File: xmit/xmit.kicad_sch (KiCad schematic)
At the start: 38 parts

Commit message: First round WIP on the filters and amplifier
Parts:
- removed C1, C13, C2: 1n, symbol Device:C
- removed C10: 9p, symbol Device:C
- removed C11, C3: 120p, symbol Device:C
- removed C12, C4: 50p, symbol Device:C
- removed C14, C18: 220p, symbol Device:C
- removed C15: 12p, symbol Device:C
- removed C16: 330p, symbol Device:C
- removed C17: 31p, symbol Device:C
- removed C5: 8.1p, symbol Device:C
- removed C6: 3.9p, symbol Device:C
- removed C7: 200p, symbol Device:C
- removed C8: 81p, symbol Device:C
- removed C9: 18p, symbol Device:C
- removed L1, L3: 1600n, symbol Device:L
- removed L2, L4: 800n, symbol Device:L
- removed L5: 2200n, symbol Device:L
- removed L6: 2000n, symbol Device:L
- removed R10, R11, R14, R15, R4, R5: 1e9, symbol Device:R
- removed R12, R6: 10, symbol Device:R
- removed R13, R3, R9: 10k, symbol Device:R
- removed R7: 150, symbol Device:R
- removed R8: 200, symbol Device:R
- removed V2: VPULSE, symbol Simulation_SPICE:VPULSE
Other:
- added sheet power (power.kicad_sch)
- added sheet transmit filters (filter.kicad_sch)

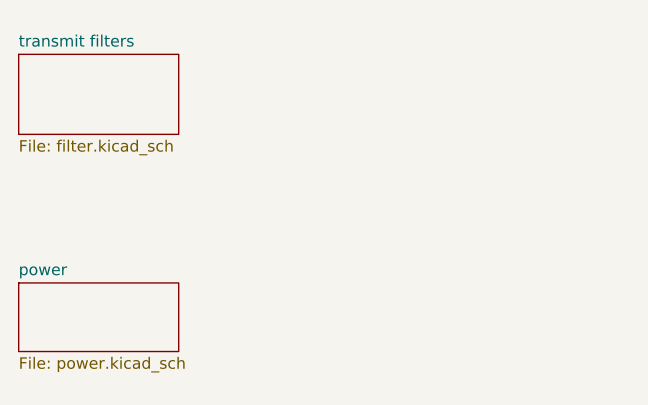
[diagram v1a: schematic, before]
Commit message: WIP commit, but the circuit is nearly done and PCB is beginning for form.
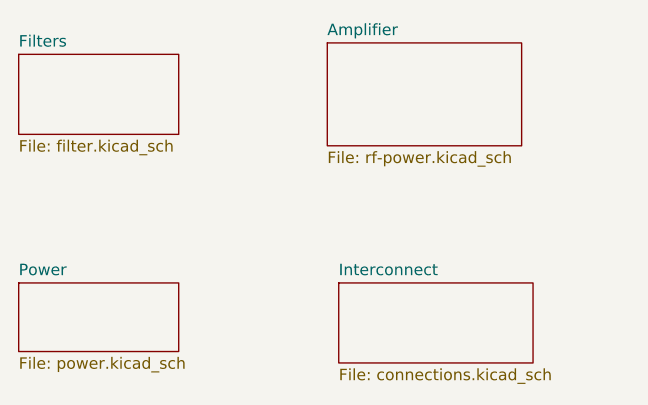
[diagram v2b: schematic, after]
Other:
- sheet power renamed Power
- sheet transmit filters renamed Filters
- added sheet Amplifier (rf-power.kicad_sch)
- added sheet Interconnect (connections.kicad_sch)
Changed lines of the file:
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@@
 	(paper "A4")
+	(sheet
+		(at 179.07 49.53)
+		(size 21.59 11.43)
+		(exclude_from_sim no)
+		(in_bom yes)
+		(on_board yes)
+		(dnp no)
+		(fields_autoplaced yes)
+		(stroke
+			(width 0.1524)
+			(type solid)
+		)
+		(fill
+			(color 0 0 0 0)
+		)
+		(property "Sheetname" "Amplifier"
+			(at 179.07 48.8184 0)
+			(show_name no)
+			(do_not_autoplace no)
+			(effects
+				(font
+					(size 1.27 1.27)
+				)
+				(justify left bottom)
+			)
+		)
+		(property "Sheetfile" "rf-power.kicad_sch"
+			(at 179.07 61.5446 0)
+			(show_name no)
+			(do_not_autoplace no)
+			(effects
+				(font
+					(size 1.27 1.27)
+				)
+				(justify left top)
+			)
+		)
+		(instances
+			(project "xmit"
+				(path "/938afe95-c1c4-4cca-88b7-71a9df9e4417"
+					(page "4")
+				)
+			)
+		)
+	)
+	(sheet
+		(at 180.34 76.2)
+		(size 21.59 8.89)
+		(exclude_from_sim no)
+		(in_bom yes)
+		(on_board yes)
+		(dnp no)
+		(fields_autoplaced yes)
+		(stroke
+			(width 0.1524)
+			(type solid)
+		)
+		(fill
+			(color 0 0 0 0)
+		)
+		(property "Sheetname" "Interconnect"
+			(at 180.34 75.4884 0)
+			(show_name no)
+			(do_not_autoplace no)
+			(effects
+				(font
+					(size 1.27 1.27)
+				)
+				(justify left bottom)
+			)
+		)
+		(property "Sheetfile" "connections.kicad_sch"
+			(at 180.34 85.6746 0)
+			(show_name no)
+			(do_not_autoplace no)
+			(effects
+				(font
+					(size 1.27 1.27)
+				)
+				(justify left top)
+			)
+		)
+		(instances
+			(project "xmit"
+				(path "/938afe95-c1c4-4cca-88b7-71a9df9e4417"
+					(page "5")
+				)
+			)
+		)
+	)
 	(sheet
 		(at 144.78 50.8)
@@
 			(color 0 0 0 0)
 		)
-		(property "Sheetname" "transmit filters"
+		(property "Sheetname" "Filters"
 			(at 144.78 50.0884 0)
 			(show_name no)
@@
 			(color 0 0 0 0)
 		)
-		(property "Sheetname" "power"
+		(property "Sheetname" "Power"
 			(at 144.78 75.4884 0)
 			(show_name no)
